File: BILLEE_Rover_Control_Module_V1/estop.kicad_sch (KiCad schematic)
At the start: 5 parts, among them SW1 ESTOP, U1 Screw Terminal, U2 SN74LVC08APWR, U3 SN74LVC08APWR, U4 SN74LVC08APWR

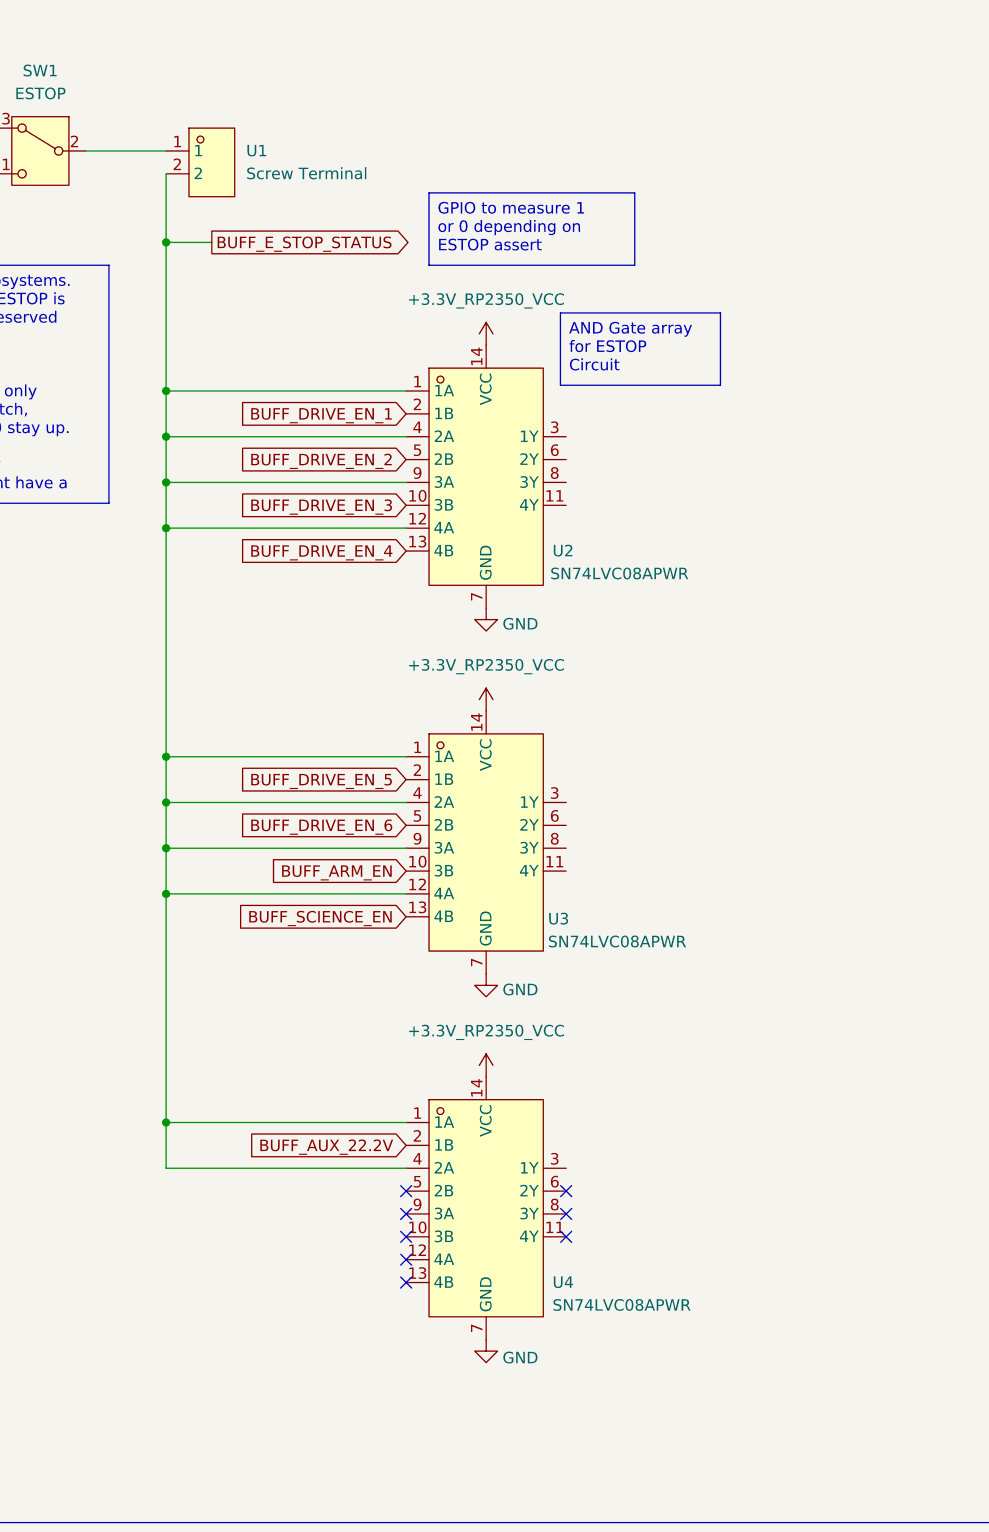
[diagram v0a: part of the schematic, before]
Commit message: Implemented Logic Subsystem
Implemented all of the Logic subsystem, missing reverse circuit protection.
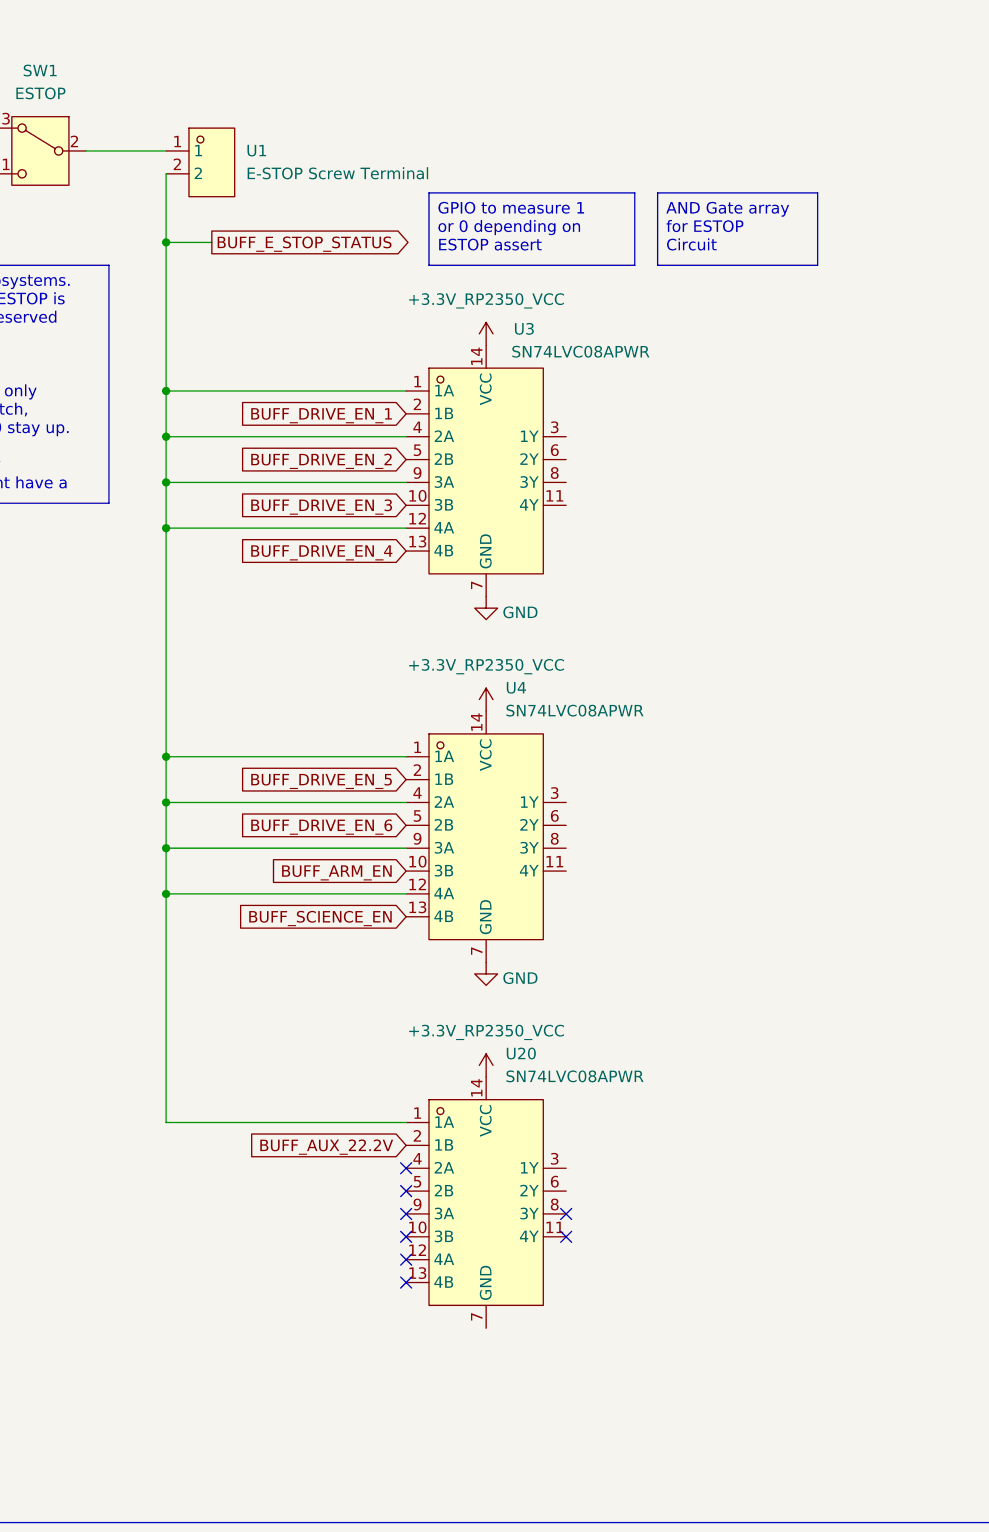
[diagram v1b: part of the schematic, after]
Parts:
- removed U1: Screw Terminal, PDB_LCSC:CONN-TH_P5.00_KF301-5.0-2P, symbol PDB_LSCS_Libs:KF301-5.0-2P
- removed U2, U3, U4: SN74LVC08APWR, PDB_LCSC:TSSOP-14_L5.0-W4.4-P0.65-LS6.4-BL, symbol PDB_LSCS_Libs:SN74LVC08APWR
- added U1: E-STOP Screw Terminal, PDB_LCSC:CONN-TH_P5.00_KF301-5.0-2P, symbol PDB_LCSC_Libs:KF301-5.0-2P
- added U20, U3, U4: SN74LVC08APWR, PDB_LCSC:TSSOP-14_L5.0-W4.4-P0.65-LS6.4-BL, symbol PDB_LCSC_Libs:SN74LVC08APWR
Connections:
- net +3.3V_RP2350_VCC: now also U20.14 (VCC), U3.14 (VCC), U4.14 (VCC)
- net BUFF_ARM_EN: now also U4.10 (3B)
- net BUFF_AUX_22.2V: now also U20.2 (1B)
- net BUFF_DRIVE_EN_1: now also U3.2 (1B)
- net BUFF_DRIVE_EN_2: now also U3.5 (2B)
- net BUFF_DRIVE_EN_3: now also U3.10 (3B)
- net BUFF_DRIVE_EN_4: now also U3.13 (4B)
- net BUFF_DRIVE_EN_5: now also U4.2 (1B)
- net BUFF_DRIVE_EN_6: now also U4.5 (2B)
- net BUFF_E_STOP_STATUS: now also U1.2, U20.1 (1A), U3.1 (1A), U3.12 (4A), U3.4 (2A), U3.9 (3A), U4.1 (1A), U4.12 (4A), U4.4 (2A), U4.9 (3A)
- net BUFF_SCIENCE_EN: now also U4.13 (4B)
- net GND: now also U3.7 (GND), U4.7 (GND)
- net at SW1.2 (B): now also U1.1

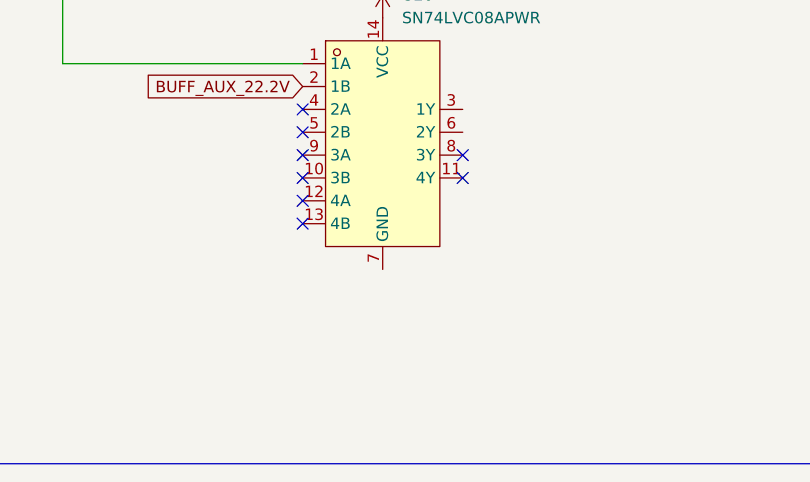
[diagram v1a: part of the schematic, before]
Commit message: Firmware Updated
INAManager, MCPManager, FPManager. Remove resistor on ESTOP BUFFER.
FPManager still needs a state machine to technically do this correctly, I dont want to rely too much on the cpp implementation
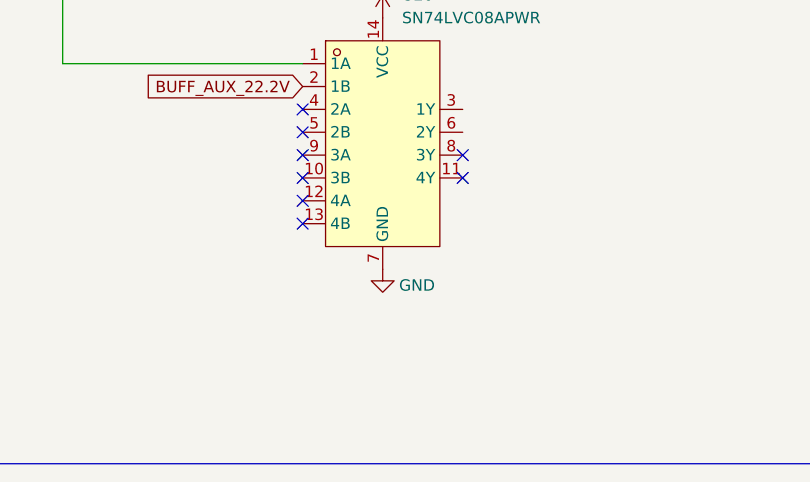
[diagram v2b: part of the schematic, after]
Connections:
- net GND: now also U20.7 (GND)
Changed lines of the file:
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@@
+	(symbol
+		(lib_id "power:GND")
+		(at 93.98 173.99 0)
+		(unit 1)
+		(body_style 1)
+		(exclude_from_sim no)
+		(in_bom yes)
+		(on_board yes)
+		(in_pos_files yes)
+		(dnp no)
+		(property "Reference" "#PWR0109"
+			(at 93.98 180.34 0)
+			(hide yes)
+			(show_name no)
+			(do_not_autoplace no)
+			(effects
+				(font
+					(size 1.27 1.27)
+				)
+			)
+		)
+		(property "Value" "GND"
+			(at 97.79 175.768 0)
+			(show_name no)
+			(do_not_autoplace no)
+			(effects
+				(font
+					(size 1.27 1.27)
+				)
+			)
+		)
+		(property "Footprint" ""
+			(at 93.98 173.99 0)
+			(hide yes)
+			(show_name no)
+			(do_not_autoplace no)
+			(effects
+				(font
+					(size 1.27 1.27)
+				)
+			)
+		)
+		(property "Datasheet" ""
+			(at 93.98 173.99 0)
+			(hide yes)
+			(show_name no)
+			(do_not_autoplace no)
+			(effects
+				(font
+					(size 1.27 1.27)
+				)
+			)
+		)
+		(property "Description" "Power symbol creates a global label with name \"GND\" , ground"
+			(at 93.98 173.99 0)
+			(hide yes)
+			(show_name no)
+			(do_not_autoplace no)
+			(effects
+				(font
+					(size 1.27 1.27)
+				)
+			)
+		)
+		(pin "1"
+		)
+		(instances
+			(project "BILLEE_Rover_Control_Module_V1"
+				(path "/e701dc98-f022-461d-84b5-6b2dd8d89d58/38c7de8f-1e1e-425a-b64c-5257d5cddadc"
+					(reference "#PWR0109")
+					(unit 1)
+				)
+			)
+		)
+	)
 	(symbol
 		(lib_id "power:GND")

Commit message: WIP Checkpoint
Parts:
- removed U20: SN74LVC08APWR, PDB_LCSC:TSSOP-14_L5.0-W4.4-P0.65-LS6.4-BL, symbol PDB_LCSC_Libs:SN74LVC08APWR
- added C28, C32, C45, C50, C51, C52, C58, C59: 4.7u, Capacitor_SMD:C_0402_1005Metric, symbol Device:C
- added C29, C33, C46, C53, C54, C55, C60, C61: 0.47u, Capacitor_SMD:C_0402_1005Metric, symbol Device:C
- added C30, C31, C34, C47, C48, C49, C56, C57: 47u, Capacitor_SMD:C_0402_1005Metric, symbol Device:C
- added CN10, CN11, CN12, CN3, CN4, CN5, CN6, CN7, CN8, CN9: XT60PW-M, PDB_LCSC:CONN-TH_XT60PW-M, symbol PDB_LCSC_Libs:XT60PW-M
- added D2, D3, D4, D5, D6, D7, D8, D9: MBR30200CT, PDB_LCSC:TO-220-3_L10.0-W4.5-P2.54-L-1, symbol PDB_LCSC_Libs:MBR30200CT_C7502759
- added Q1, Q2, Q3, Q4, Q5, Q6, Q7, Q8: IPT007N06N, PDB_LCSC:HSOF-8_IPT007N06N, symbol PDB_LCSC_Libs:IPT007N06N
- added R24, R53, R57, R76, R77, R78, R86, R87: 200k, symbol Device:R_US
- added R48, R54, R58, R79, R80, R81, R88, R89: 10, symbol Device:R_US
- added R49, R51, R55, R60, R71, R74, R82, R84: 590k, symbol Device:R_US
- added R50, R52, R56, R70, R73, R75, R83, R85: 12.1k, symbol Device:R_US
- added U11, U13, U26, U28, U29, U30, U34, U35: LTC7001IMSE#PBF, PDB_LCSC:MSOP-10_L3.0-W3.0-P0.50-LS4.9-BL-EP, symbol PDB_LCSC_Libs:LTC7001IMSE#PBF
- added U12, U14, U27, U31, U32, U33, U36, U37: INA780BIDEKR, PDB_LCSC:VQFN-15_L6.0-W6.0-P0.60-TL, symbol PDB_LCSC_Libs:INA780BIDEKR
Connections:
- net +3.3V_RP2350_VCC: now also U12.12 (VS), U14.12 (VS), U14.4 (A0), U27.12 (VS), U31.12 (VS), U31.3 (A1), U32.12 (VS), U32.3 (A1), U32.4 (A0), U33.12 (VS), U33.4 (A0), U36.12 (VS), U36.3 (A1), U36.4 (A0), U37.12 (VS), U37.4 (A0)
- net GND: now also C30.2, C31.2, C34.2, C47.2, C48.2, C49.2, C56.2, C57.2, CN10.1 (-), CN10.3, CN10.4, CN11.1 (-), CN11.3, CN11.4, CN12.1 (-), CN12.3, CN12.4, CN3.1 (-), CN3.3, CN3.4, CN4.1 (-), CN4.3, CN4.4, CN5.1 (-), CN5.3, CN5.4, CN6.1 (-), CN6.3, CN6.4, CN7.1 (-), CN7.3, CN7.4, CN8.1 (-), CN8.3, CN8.4, CN9.1 (-), CN9.3, CN9.4, D2.1, D2.3, D3.1, D3.3, D4.1, D4.3, D5.1, D5.3, D6.1, D6.3, D7.1, D7.3, D8.1, D8.3, D9.1, D9.3, R48.1, R50.1, R52.1, R54.1, R56.1, R58.1, R70.1, R73.1, R75.1, R79.1, R80.1, R81.1, R83.1, R85.1, R88.1, R89.1, U11.11 (GND), U11.3 (GND), U12.13 (GND), U12.3 (A1), U12.4 (A0), U13.11 (GND), U13.3 (GND), U14.13 (GND), U14.3 (A1), U26.11 (GND), U26.3 (GND), U27.13 (GND), U27.3 (A1), U28.11 (GND), U28.3 (GND), U29.11 (GND), U29.3 (GND), U30.11 (GND), U30.3 (GND), U31.13 (GND), U31.4 (A0), U32.13 (GND), U33.13 (GND), U34.11 (GND), U34.3 (GND), U35.11 (GND), U35.3 (GND), U36.13 (GND), U37.13 (GND)
- net GATE_DRIVE4: now reaches U3.11 (4Y)
- net GATE_DRIVE4: now also U28.4 (INP)
- net GATE_DRIVE1: now reaches U3.3 (1Y)
- net GATE_DRIVE1: now also U11.4 (INP)
- net GATE_DRIVE2: now reaches U3.6 (2Y)
- net GATE_DRIVE2: now also U13.4 (INP)
- net GATE_DRIVE3: now reaches U3.8 (3Y)
- net GATE_DRIVE3: now also U26.4 (INP)
- net GATE_SCIENCE: now reaches U4.11 (4Y)
- net GATE_SCIENCE: now also U35.4 (INP)
- net GATE_DRIVE5: now reaches U4.3 (1Y)
- net GATE_DRIVE5: now also U29.4 (INP)
- net GATE_DRIVE6: now reaches U4.6 (2Y)
- net GATE_DRIVE6: now also U30.4 (INP)
- net GATE_ARM: now reaches U4.8 (3Y)
- net GATE_ARM: now also U34.4 (INP)
- new net: U14.1 (SH+), U14.2 (IN+)
- new net: U14.10 (IN–), U14.9 (SH–)
- new net: R57.1, U26.7 (TGUP)
- new net: C46.1, Q3.1 (G), R57.2, U26.6 (TGDN)
- new net: C54.1, Q5.1 (G), R77.2, U29.6 (TGDN)
- new net: C54.2, R80.2
- new net: C60.1, Q7.1 (G), R86.2, U34.6 (TGDN)
- new net: C60.2, R88.2
- new net: R74.1, R75.2, U30.5 (OVLO)
- new net: C55.1, Q6.1 (G), R78.2, U30.6 (TGDN)
- new net: R78.1, U30.7 (TGUP)
- new net: C52.2, D7.2, U30.8 (TS)
- new net: C52.1, U30.9 (BST)
- new net: U37.1 (SH+), U37.2 (IN+)
- new net: U37.10 (IN–), U37.9 (SH–)
- new net: C61.1, Q8.1 (G), R87.2, U35.6 (TGDN)
- new net: C61.2, R89.2
- new net: C33.1, Q2.1 (G), R53.2, U13.6 (TGDN)
- new net: C32.1, U13.9 (BST)
- new net: C32.2, D3.2, U13.8 (TS)
- new net: C46.2, R58.2
- new net: C45.1, U26.9 (BST)
- new net: C45.2, D4.2, U26.8 (TS)
- new net: C53.2, R79.2
- new net: U32.1 (SH+), U32.2 (IN+)
- new net: U32.10 (IN–), U32.9 (SH–)
- new net: R71.1, R73.2, U29.5 (OVLO)
- new net: R77.1, U29.7 (TGUP)
- new net: C51.2, D6.2, U29.8 (TS)
- new net: C51.1, U29.9 (BST)
- new net: R86.1, U34.7 (TGUP)
- new net: R55.1, R56.2, U26.5 (OVLO)
- new net: U31.1 (SH+), U31.2 (IN+)
- new net: U31.10 (IN–), U31.9 (SH–)
- new net: C58.2, D8.2, U34.8 (TS)
- new net: R24.1, U11.7 (TGUP)
- new net: C29.1, Q1.1 (G), R24.2, U11.6 (TGDN)
- new net: R82.1, R83.2, U34.5 (OVLO)
- new net: C58.1, U34.9 (BST)
- new net: R49.1, R50.2, U11.5 (OVLO)
- new net: C28.2, D2.2, U11.8 (TS)
- new net: C28.1, U11.9 (BST)
- new net: R87.1, U35.7 (TGUP)
- new net: C55.2, R81.2
- new net: R84.1, R85.2, U35.5 (OVLO)
- new net: U12.1 (SH+), U12.2 (IN+)
- new net: U12.10 (IN–), U12.9 (SH–)
- new net: U36.1 (SH+), U36.2 (IN+)
- new net: U36.10 (IN–), U36.9 (SH–)
- new net: R60.1, R70.2, U28.5 (OVLO)
- new net: C29.2, R48.2
- new net: R51.1, R52.2, U13.5 (OVLO)
- new net: C53.1, Q4.1 (G), R76.2, U28.6 (TGDN)
- new net: R76.1, U28.7 (TGUP)
- new net: C50.2, D5.2, U28.8 (TS)
- new net: C50.1, U28.9 (BST)
- new net: R53.1, U13.7 (TGUP)
- new net: U33.1 (SH+), U33.2 (IN+)
- new net: U33.10 (IN–), U33.9 (SH–)
- new net: C59.1, U35.9 (BST)
- new net: C59.2, D9.2, U35.8 (TS)
- new net: C33.2, R54.2
- new net: U27.1 (SH+), U27.2 (IN+)
- new net: U27.10 (IN–), U27.9 (SH–)
- new net +12V_AUX_VCC: U11.1 (VCC), U13.1 (VCC), U26.1 (VCC), U28.1 (VCC), U29.1 (VCC), U30.1 (VCC), U34.1 (VCC), U35.1 (VCC)
- new net +14.4V_ARM: Q7.2 (S), U36.14 (VBUS), U36.15 (IS+)
- new net +14.4V_ARM/SCIENCE_BATT: C56.1, C57.1, CN12.2 (+), Q7.3 (D), Q8.3 (D), R82.2, R84.2
- new net +14.4V_ARM_SENSOR_OUT: CN10.2 (+), U36.8 (IS–)
- new net +14.4V_DRIVE1: Q1.2 (S), U12.14 (VBUS), U12.15 (IS+)
- new net +14.4V_DRIVE1_SENSOR_OUT: CN3.2 (+), U12.8 (IS–)
- new net +14.4V_DRIVE2: Q2.2 (S), U14.14 (VBUS), U14.15 (IS+)
- new net +14.4V_DRIVE2_SENSOR_OUT: CN5.2 (+), U14.8 (IS–)
- new net +14.4V_DRIVE3: Q3.2 (S), U27.14 (VBUS), U27.15 (IS+)
- new net +14.4V_DRIVE3_SENSOR_OUT: CN6.2 (+), U27.8 (IS–)
- new net +14.4V_DRIVE4: Q4.2 (S), U31.14 (VBUS), U31.15 (IS+)
- new net +14.4V_DRIVE4_SENSOR_OUT: CN7.2 (+), U31.8 (IS–)
- new net +14.4V_DRIVE5: Q5.2 (S), U32.14 (VBUS), U32.15 (IS+)
- new net +14.4V_DRIVE5_SENSOR_OUT: CN8.2 (+), U32.8 (IS–)
- new net +14.4V_DRIVE6: Q6.2 (S), U33.14 (VBUS), U33.15 (IS+)
- new net +14.4V_DRIVE6_SENSOR_OUT: CN9.2 (+), U33.8 (IS–)
- new net +14.4V_DRIVE_BATT: C30.1, C31.1, C34.1, C47.1, C48.1, C49.1, CN4.2 (+), Q1.3 (D), Q2.3 (D), Q3.3 (D), Q4.3 (D), Q5.3 (D), Q6.3 (D), R49.2, R51.2, R55.2, R60.2, R71.2, R74.2
- new net +14.4V_SCIENCE: Q8.2 (S), U37.14 (VBUS), U37.15 (IS+)
- new net +14.4V_SCIENCE_SENSOR_OUT: CN11.2 (+), U37.8 (IS–)
- new net BUFF_SCL_0: U12.6 (SCL), U14.6 (SCL), U27.4 (A0), U27.6 (SCL), U31.6 (SCL), U32.6 (SCL), U33.3 (A1), U33.6 (SCL), U36.6 (SCL), U37.3 (A1), U37.6 (SCL)
- new net BUFF_SDA_0: U12.5 (SDA), U14.5 (SDA), U27.5 (SDA), U31.5 (SDA), U32.5 (SDA), U33.5 (SDA), U36.5 (SDA), U37.5 (SDA)
- no-connect marks 8 -> 32
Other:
- note added: "Arm/Science Power Control and Monitoring"
- note added: "Drivetrain Power Control and Monitoring"
- note added: "ESTOP Gating"
- note removed: "ESTOP / Power Circuit"
- moved on the sheet: SW1, U1, U3, U4

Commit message: Goodies
Updated all schematics
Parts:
- added U39, U40: MCP9808T-E/MS, PDB_LCSC:MSOP-8_L3.0-W3.0-P0.65-LS4.9-BL, symbol PDB_LCSC_Libs:MCP9808T-E_MS
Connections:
- net +3.3V_RP2350_VCC: now also U39.7 (A0), U39.8 (VDD), U40.7 (A0), U40.8 (VDD)
- net GND: now also U39.4 (GND), U39.5 (A2), U39.6 (A1), U40.4 (GND), U40.5 (A2), U40.6 (A1)
- new net BUFF_SCL_1: U39.2 (SCL), U40.2 (SCL)
- new net BUFF_SDA_1: U39.1 (SDA), U40.1 (SDA)
- no-connect marks 32 -> 34
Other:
- note added: "Arm/Science Temp Sense"
- note added: "Drivetrain Temp Sense"
- company: (none) -> Bronco STAR
- title: (none) -> BILLEE_RCM

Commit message: more goodies
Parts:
- removed CN12, CN4: XT60PW-M, PDB_LCSC:CONN-TH_XT60PW-M, symbol PDB_LCSC_Libs:XT60PW-M
- removed SW1: ESTOP, Button_Switch_SMD:Nidec_Copal_CAS-120A, symbol Switch:SW_Nidec_CAS-120A1
- added CN12, CN2, CN4: XT90PW-M.G.Y, PDB_LCSC:CONN-TH_XT90PW-M.G.Y, symbol PDB_LCSC_Libs:XT90PW-M.G.Y
- added CN13: XT60PW-M, PDB_LCSC:CONN-TH_XT60PW-M, symbol PDB_LCSC_Libs:XT60PW-M
- U1: value E-STOP Screw Terminal -> Screw Terminal for ESTOP - NC
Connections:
- net +14.4V_ARM_SENSOR_OUT: now also CN13.2 (+)
- net +14.4V_DRIVE_BATT: now also CN2.1 (+)
- net +3.3V_RP2350_VCC: now also U1.2
- net BUFF_E_STOP_STATUS: now also U1.1; no longer U1.2
- net GND: now also CN12.2 (-), CN12.3, CN12.4, CN13.1 (-), CN13.3, CN13.4, CN2.2 (-), CN2.3, CN2.4, CN4.2 (-), CN4.3, CN4.4
- net +14.4V_ARM/SCIENCE_BATT renamed +14.4V_ARM_BATT
- net +14.4V_ARM_BATT: now also CN4.1 (+); no longer C57.1, Q8.3 (D), R84.2
- new net +14.4V_SCIENCE_BATT: C57.1, CN12.1 (+), Q8.3 (D), R84.2
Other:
- note added: "ARM"
- note added: "SCIENCE"
- moved on the sheet: C56, C57, C58, C59, C60, C61, CN10, CN11, D8, D9, Q7, Q8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

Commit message: Updated for schematic review by claude
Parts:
- R49, R51, R55, R60, R71, R74, R82, R84: value 590k -> 840k
- R50, R52, R56, R70, R73, R75, R83, R85: value 12.1k -> 33k

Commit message: Applied first round of Claude review suggestions.
Updated UVLO and OVLO guidelines.
Updated symbol pin mappings and net attributes. Preparing for layout
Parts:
- added R90: 10k, symbol Device:R_US
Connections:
- net +3.3V_RP2350_VCC: now also U1.1; no longer U1.2
- net BUFF_E_STOP_STATUS: now also U1.2, R90.2; no longer U1.1
- net GND: now also R90.1

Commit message: More goodies.
Did a review with claude and patched a lot of missng things. Updated RCP for LOGIC and more.
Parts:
- added C66, C67, C68, C69, C70, C71: 47u, symbol Device:C
- added R91, R92, R93, R94, R95, R96, R97, R98: 150k, symbol Device:R_US
- U1: value Screw Terminal for ESTOP - NC -> Screw Terminal for ESTOP - NO
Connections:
- net +14.4V_ARM_SENSOR_OUT: now also C66.1, C67.1, C68.1
- net +14.4V_SCIENCE_SENSOR_OUT: now also C69.1, C70.1, C71.1
- net +3.3V_RP2350_VCC: now also U33.3 (A1), U40.6 (A1); no longer U33.4 (A0), U40.7 (A0)
- net BUFF_SCL_0: now also U33.4 (A0); no longer U33.3 (A1)
- net GND: now also U40.7 (A0), C66.2, C67.2, C68.2, C69.2, C70.2, C71.2, R91.1, R92.1, R93.1, R94.1, R95.1, R96.1, R97.1, R98.1; no longer U40.6 (A1)
- net at U30.2 (VCCUV): now also R97.2
- net at U29.2 (VCCUV): now also R96.2
- net at U34.2 (VCCUV): now also R91.2
- net at U11.2 (VCCUV): now also R93.2
- net at U28.2 (VCCUV): now also R98.2
- net at U26.2 (VCCUV): now also R95.2
- net at U35.2 (VCCUV): now also R92.2
- net at U13.2 (VCCUV): now also R94.2
- no-connect marks 34 -> 26
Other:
- moved on the sheet: U36
